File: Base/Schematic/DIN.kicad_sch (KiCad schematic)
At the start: 28 parts, among them U12 LM239DR2G, U13 LM239DR2G, U14 LM239DR2G, U15 LM239DR2G

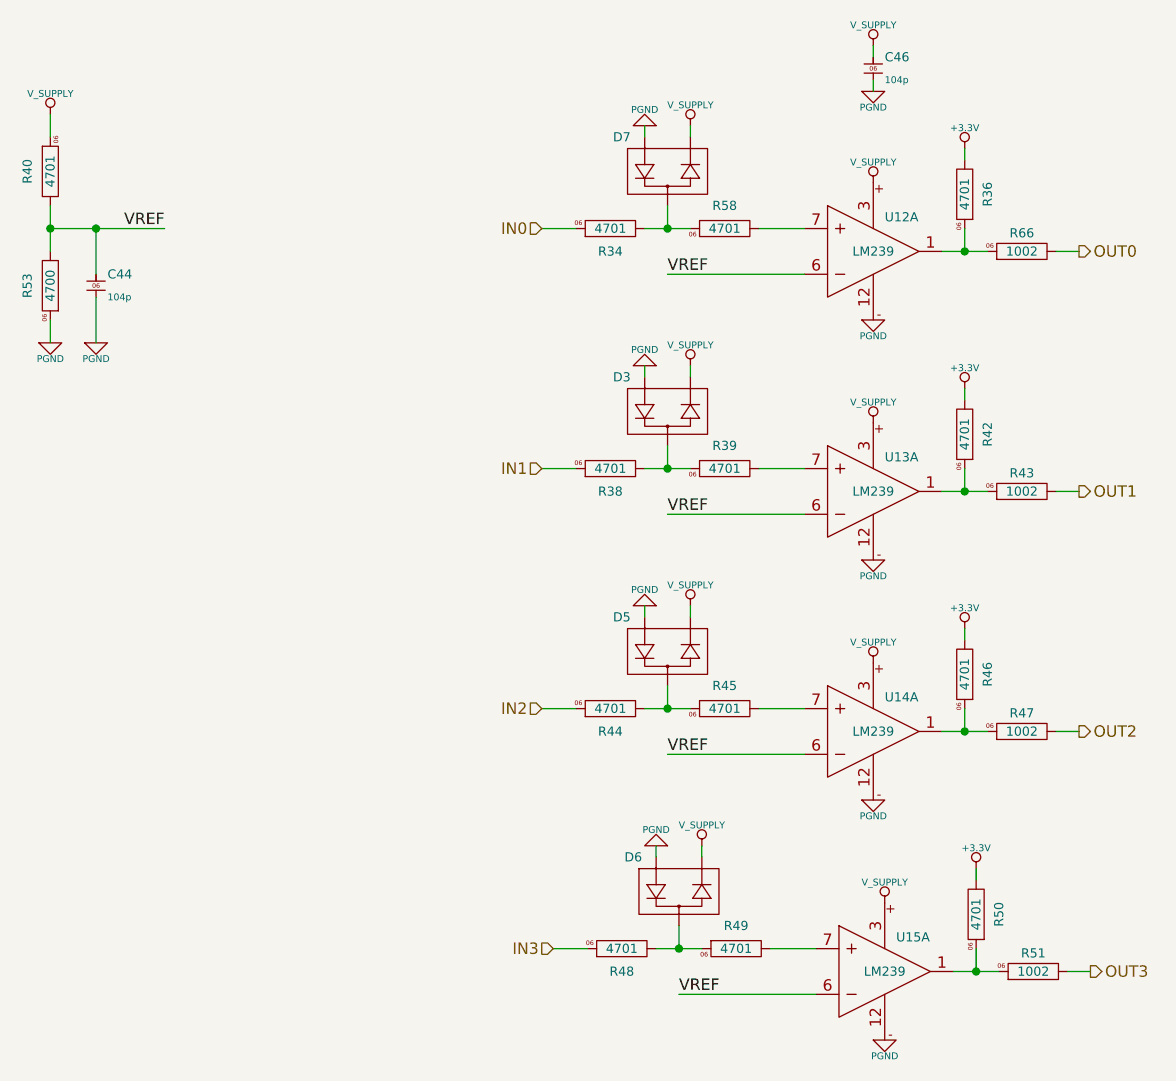
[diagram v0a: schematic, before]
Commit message: [Base 회로도 업데이트] - AIN 입력 4개 추가
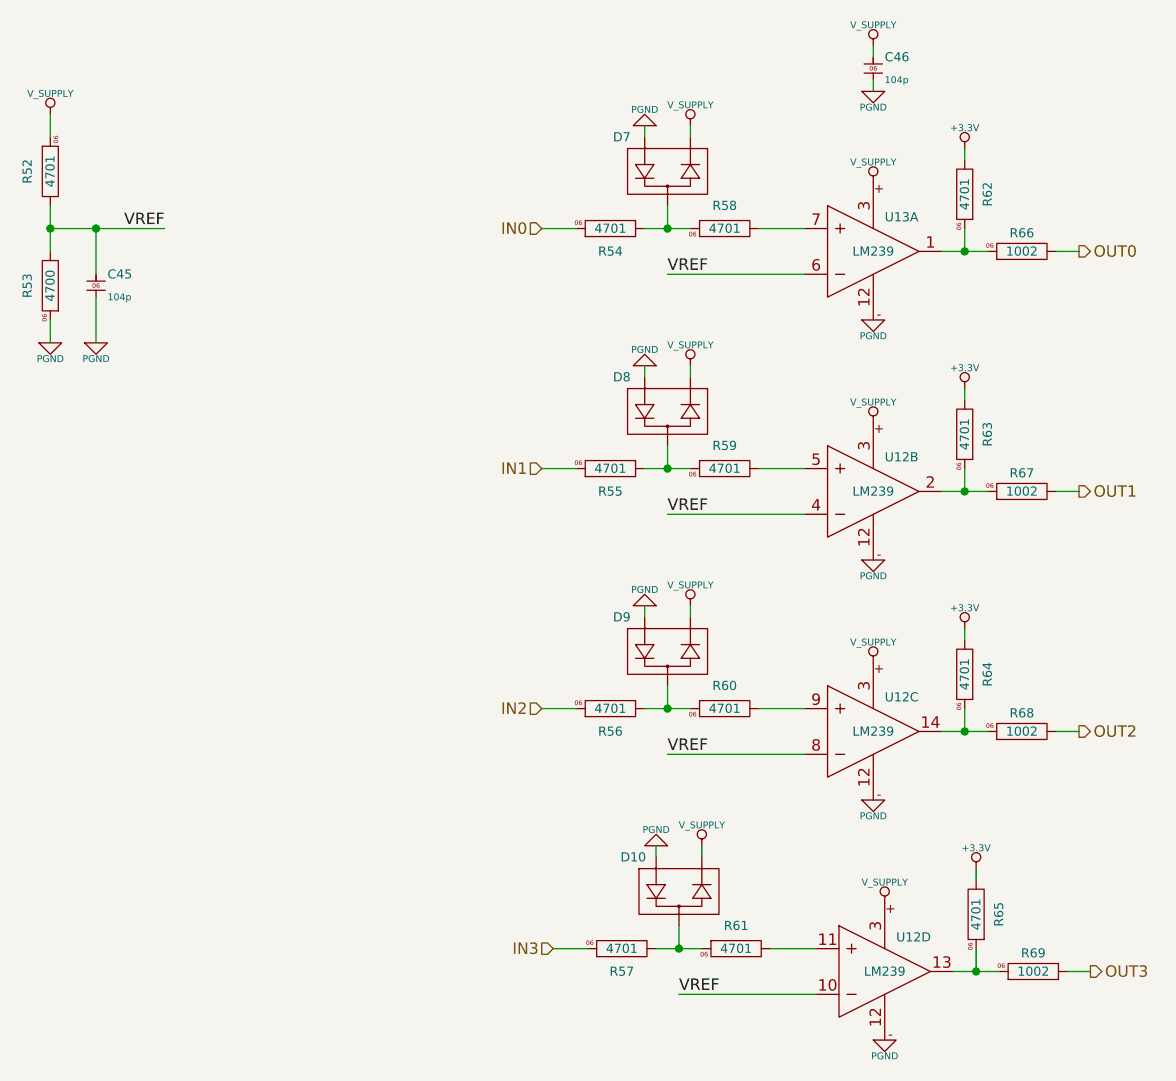
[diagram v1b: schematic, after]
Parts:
- renumbered C44 to C45, D6 to D10, D3 to D8, D5 to D9, R40 to R52, R34 to R54, R38 to R55, R44 to R56, R48 to R57, R39 to R59, R45 to R60, R49 to R61, R36 to R62, R42 to R63, R46 to R64, R50 to R65, R43 to R67, R47 to R68, R51 to R69, U14 to U12, U13 to U12, U15 to U12, U12 to U13
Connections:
- net VREF: now also U12.10 (-), U12.4 (-), U12.8 (-); no longer U12.6 (-), U12.6 (-), U12.6 (-)
- net at R64.1, R68.1: now also U12.14 (OUT); no longer U12.1 (OUT)
- net at R60.2: now also U12.9 (+); no longer U12.7 (+)
- net at R65.1, R69.1: now also U12.13 (OUT); no longer U12.1 (OUT)
- net at R59.2: now also U12.5 (+); no longer U12.7 (+)
- net at R63.1, R67.1: now also U12.2 (OUT); no longer U12.1 (OUT)
- net at R61.2: now also U12.11 (+); no longer U12.7 (+)
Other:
- company: (none) -> -
- title: (none) -> Open-PLC-Project
